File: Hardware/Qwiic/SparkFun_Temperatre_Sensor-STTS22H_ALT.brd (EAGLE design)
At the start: 25.4 x 25.4 mm, 54 parts, among them J1 QWIIC_RIGHT_ANGLE, J2 QWIIC_RIGHT_ANGLE, U2 STTS22H

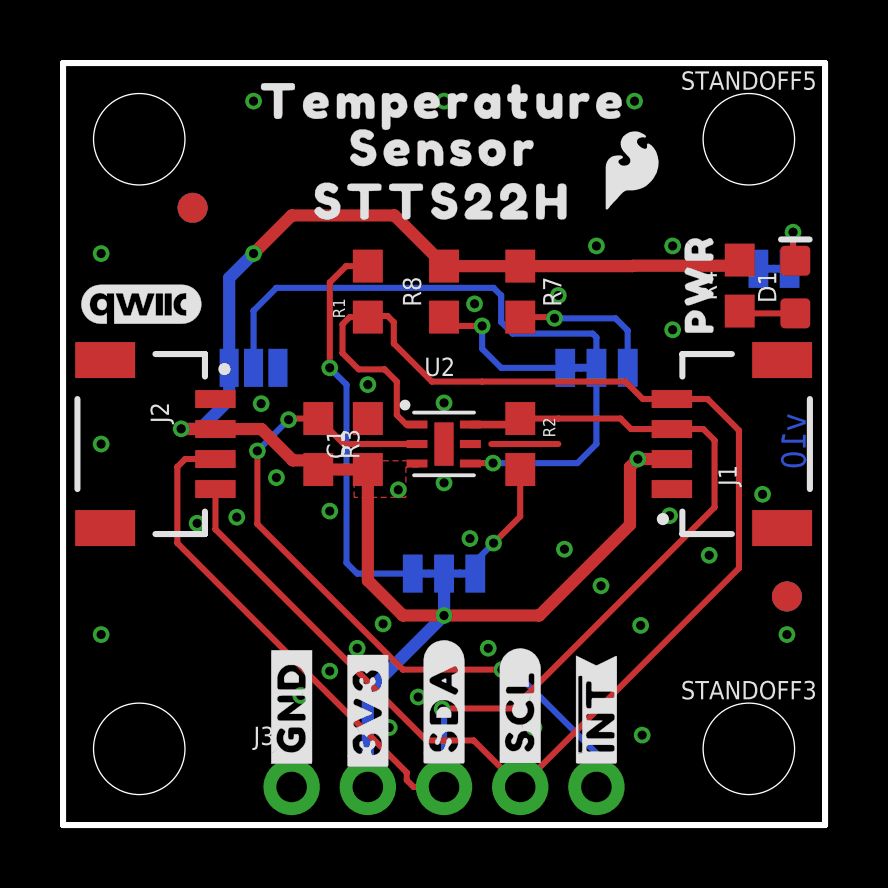
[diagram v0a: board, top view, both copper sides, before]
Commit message: Adds alternative board with exposed copper on the underside
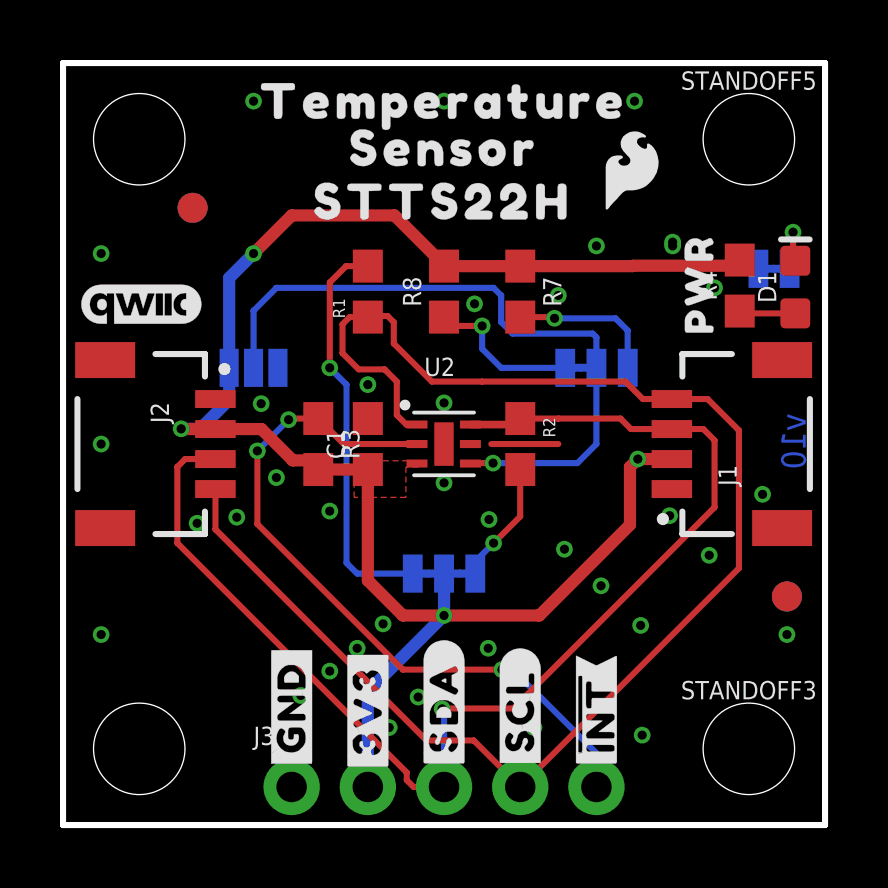
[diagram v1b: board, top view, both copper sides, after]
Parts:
- moved LOGO2 21.3 mm to (4.47, 5.70)
- moved U$8 0.18 mm to (6.38, 16.7)
- moved U$25 0.13 mm to (12.7, 6.86)
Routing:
- net GND: vias 37 -> 38
- net 3.3V: vias 5 -> 4
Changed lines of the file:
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@@
 <layer number="28" name="bValues" color="7" fill="1" visible="no" active="yes"/>
 <layer number="29" name="tStop" color="7" fill="3" visible="no" active="yes"/>
-<layer number="30" name="bStop" color="7" fill="6" visible="no" active="yes"/>
+<layer number="30" name="bStop" color="7" fill="6" visible="yes" active="yes"/>
 <layer number="31" name="tCream" color="7" fill="4" visible="no" active="yes"/>
 <layer number="32" name="bCream" color="7" fill="5" visible="no" active="yes"/>
@@
 <layer number="40" name="bKeepout" color="1" fill="11" visible="no" active="yes"/>
 <layer number="41" name="tRestrict" color="4" fill="10" visible="no" active="yes"/>
-<layer number="42" name="bRestrict" color="1" fill="10" visible="no" active="yes"/>
+<layer number="42" name="bRestrict" color="1" fill="10" visible="yes" active="yes"/>
 <layer number="43" name="vRestrict" color="2" fill="10" visible="no" active="yes"/>
 <layer number="44" name="Drills" color="7" fill="1" visible="no" active="yes"/>
@@
 <dimension x1="2.54" y1="22.86" x2="0" y2="22.86" x3="1.27" y3="27.94" textsize="1.778" layer="47" dtype="horizontal" unit="inch"/>
 <dimension x1="6.35" y1="1.27" x2="0" y2="1.27" x3="3.175" y3="-3.81" textsize="1.778" layer="47" dtype="horizontal" unit="inch"/>
+<rectangle x1="11.557" y1="10.922" x2="13.843" y2="14.478" layer="30"/>
 </plain>
 <attributes>
@@
 <attribute name="REV" value="" x="-19.05" y="-16.51" size="1.778" layer="27" display="off"/>
 </element>
-<element name="LOGO2" library="SparkFun-Aesthetics" package="OSHW-LOGO-MINI" value="OSHW-LOGOMINI" x="23.7744" y="14.71295" smashed="yes" rot="MR0"/>
+<element name="LOGO2" library="SparkFun-Aesthetics" package="OSHW-LOGO-MINI" value="OSHW-LOGOMINI" x="4.4704" y="5.69595" smashed="yes" rot="MR0"/>
 <element name="STANDOFF1" library="SparkFun-Hardware" package="STAND-OFF-TIGHT" value="STAND-OFFTIGHT" x="2.54" y="22.86" smashed="yes"/>
 <element name="STANDOFF2" library="SparkFun-Hardware" package="STAND-OFF-TIGHT" value="STAND-OFFTIGHT" x="2.54" y="2.54" smashed="yes"/>
@@
 </element>
 <element name="U$16" library="bot" package="#LED#11" value="" x="23.622" y="16.9926" smashed="yes" rot="MR0"/>
-<element name="U$25" library="bot" package="#I2C#11" value="" x="12.7" y="6.985" smashed="yes" rot="MR0"/>
+<element name="U$25" library="bot" package="#I2C#11" value="" x="12.7" y="6.858" smashed="yes" rot="MR0"/>
 <element name="U$1" library="top" package="#GND#3" value="" x="7.62" y="3.937" smashed="yes" rot="R90"/>
 <element name="U$2" library="top" package="#3V3#4" value="" x="10.16" y="3.81" smashed="yes" rot="R90"/>
@@
 <element name="U$5" library="top" package="#SDA#7" value="" x="12.7" y="3.9116" smashed="yes" rot="MR270"/>
 <element name="U$7" library="top" package="#SCL#6" value="" x="15.24" y="3.7592" smashed="yes" rot="MR270"/>
-<element name="U$8" library="top" package="#ADDR1#9" value="" x="6.5024" y="16.5862" smashed="yes" rot="MR0"/>
+<element name="U$8" library="top" package="#ADDR1#9" value="" x="6.3754" y="16.7132" smashed="yes" rot="MR0"/>
 <element name="U$12" library="top" package="#0X3C#25" value="" x="14.4272" y="15.3416" smashed="yes" rot="MR0"/>
 <element name="U$13" library="top" package="#0X3E#25" value="" x="21.1836" y="15.3416" smashed="yes" rot="MR0"/>
@@
 <via x="19.2532" y="6.6548" extent="1-16" drill="0.3048"/>
 <via x="15.6972" y="3.2512" extent="1-16" drill="0.3048"/>
-<via x="13.5636" y="9.5504" extent="1-16" drill="0.3048"/>
+<via x="14.1986" y="10.1854" extent="1-16" drill="0.3048"/>
 <wire x1="16.51" y1="12.7" x2="14.2748" y2="12.7" width="0.2032" layer="1"/>
 <via x="10.8712" y="3.2512" extent="1-16" drill="0.3048"/>
@@
 <via x="9.8044" y="5.8928" extent="1-16" drill="0.3048"/>
 <via x="17.9324" y="7.9756" extent="1-16" drill="0.3048"/>
-<via x="20.32" y="16.51" extent="1-16" drill="0.3048"/>
+<via x="21.717" y="17.907" extent="1-16" drill="0.3048"/>
 <contactref element="C1" pad="2"/>
 <via x="17.78" y="19.304" extent="1-16" drill="0.3048"/>
@@
 <via x="16.51" y="17.653" extent="1-16" drill="0.3048"/>
 <via x="6.604" y="14.0462" extent="1-16" drill="0.3048"/>
+<via x="20.32" y="19.431" extent="1-16" drill="0.3048"/>
 </signal>
 <signal name="3.3V">
@@
 <wire x1="12.7" y1="6.985" x2="12.7" y2="8.382" width="0.4064" layer="16"/>
 <wire x1="10.16" y1="8.1534" x2="11.3284" y2="6.985" width="0.4064" layer="1"/>
-<via x="11.176" y="11.176" extent="1-16" drill="0.3048"/>
 <polygon width="0.127" layer="1" thermals="no">
 <vertex x="11.8364" y="11.938"/>
